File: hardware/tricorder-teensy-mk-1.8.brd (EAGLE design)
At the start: 50.8 x 22.9 mm, 22 parts, among them U1 MCP73831

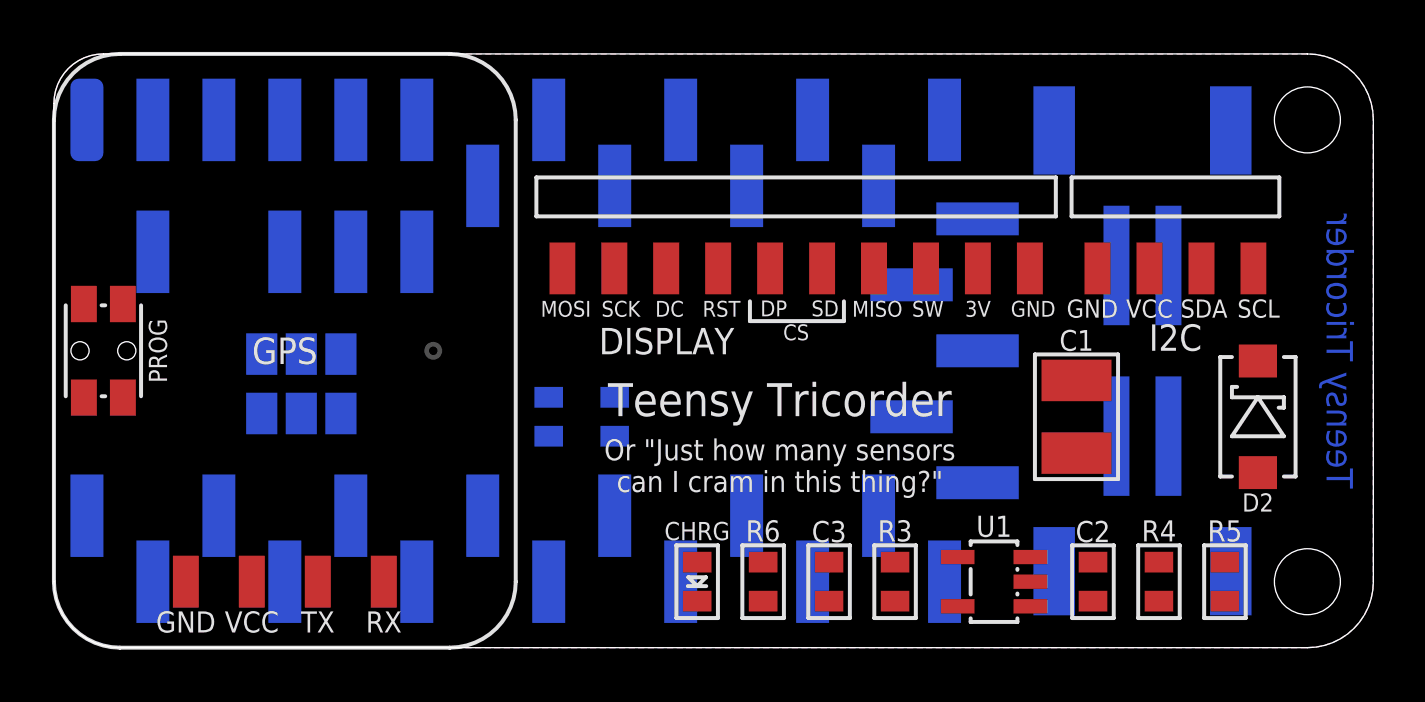
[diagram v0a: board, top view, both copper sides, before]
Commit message: rev1.8 of tricorder hat, now for teensy:
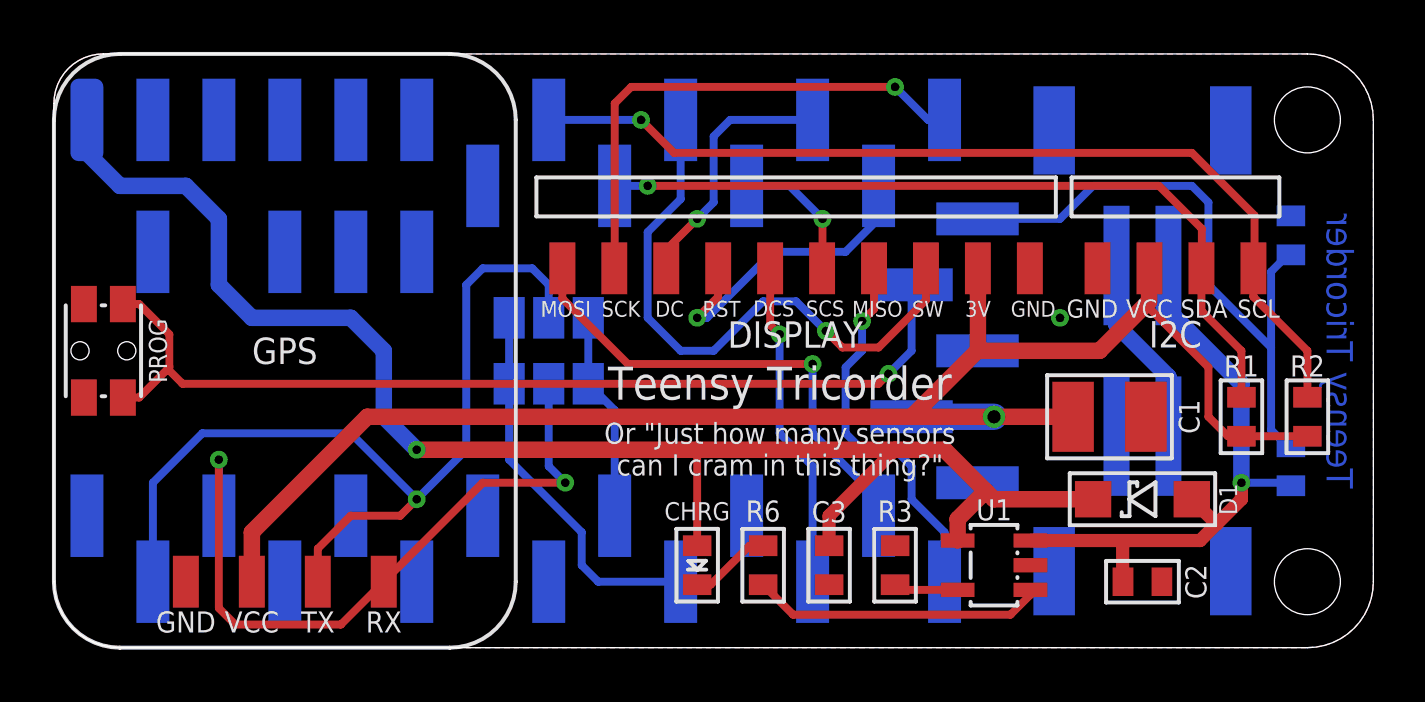
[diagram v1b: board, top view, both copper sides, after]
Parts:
- removed D2: (no value), a_parts:SMA-DIODE-SCHOTTKY
- added D1: (no value), a_parts:SOD123-SCHOTTKY
- moved R2 29.2 mm to (48.3, 8.89), flipped to the top
- moved R1 24.1 mm to (45.7, 8.89), flipped to the top
- moved R5 13.6 mm to (47.6, 15.9), flipped to the bottom
- moved GPS_TX_ALT 9.63 mm to (19.1, 12.7)
- moved GPS_RX_ALT 9.59 mm to (19.1, 10.2)
- moved R4 6.75 mm to (47.6, 6.99), flipped to the bottom, turned to 270 degrees
- moved C2 1.90 mm to (41.9, 2.54), turned to 0 degrees
- moved C1 1.27 mm to (40.6, 8.89), turned to 0 degrees
- moved C3 0.63 mm to (29.8, 3.17)
- moved CHRG 0.63 mm to (24.8, 3.17)
- moved R3 0.63 mm to (32.4, 3.17)
- moved R6 0.63 mm to (27.3, 3.17)
- moved U1 0.63 mm to (36.2, 3.17)
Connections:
- net BATT_DIV: now also TEENSY.A14/DAC; no longer TEENSY.20/A6
- net N$5: now also PWR_SW.2; no longer PWR_SW.1
- net VBAT: now also D1.A, PWR_SW.1; no longer D2.A, PWR_SW.2
- net VUSB: now also D1.C; no longer D2.C
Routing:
- net 3.3V: track 0.00 -> 63.4 mm, vias 0 -> 1
- net VUSB: track 0.00 -> 59.3 mm, vias 0 -> 1
- net PROG: track 0.00 -> 37.8 mm, vias 0 -> 1
- net SCL: track 0.00 -> 36.6 mm, vias 0 -> 1
- net GPS_TX: track 0.00 -> 35.7 mm, vias 0 -> 1
- net SDA: track 0.00 -> 30.4 mm, vias 0 -> 1
- net GPS_RX: track 0.00 -> 27.8 mm, vias 0 -> 2
- net BATT_DIV: track 0.00 -> 24.4 mm
- net VBAT: track 0.00 -> 23.8 mm, vias 0 -> 1
- net SD_SW: track 0.00 -> 22.9 mm, vias 0 -> 1
- net SCK: track 0.00 -> 19.8 mm, vias 0 -> 1
- net MOSI: track 0.00 -> 18.7 mm, vias 0 -> 1
- net MISO: track 0.00 -> 14.8 mm, vias 0 -> 1
- net 8/TX3: track 0.00 -> 14.8 mm
- net !DISP_CS: track 0.00 -> 12.7 mm, vias 0 -> 1
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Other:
- board text added: "DCS"
- board text added: "SCS"
- board text removed: "CS"
- board text removed: "DP"
- board text removed: "SD"
